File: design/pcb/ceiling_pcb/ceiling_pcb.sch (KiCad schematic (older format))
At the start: 10 parts, among them J1 Conn_01x09, J10 shock_grid, J2 Conn_01x09, J3 shock_grid, J4 shock_grid, J5 shock_grid, J6 shock_grid, J7 shock_grid, J8 shock_grid, J9 shock_grid

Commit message: Updated electrode_vertices.py to also generate electrodes interleaved along the long axis, for an orthogonal set of ceiling electrodes. New *_lengthwise footprint should be correct, if not a little wide.
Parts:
- J10, J3, J4, J5, J6, J7, J8, J9: footprint footprints:electrodes_clearance0.6mm -> footprints:electrodes_clearance0.6mm_W0.4mm_lengthwise
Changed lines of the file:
@@
 F 0 "J3" H 5378 1728 60  0000 L CNN
 F 1 "shock_grid" H 5378 1622 60  0000 L CNN
-F 2 "footprints:electrodes_clearance0.6mm" H 4350 1450 60  0001 C CNN
+F 2 "footprints:electrodes_clearance0.6mm_W0.4mm_lengthwise" H 4350 1450 60  0001 C CNN
 F 3 "" H 4350 1450 60  0001 C CNN
 	1    4350 1450
@@
 F 0 "J5" H 5378 3178 60  0000 L CNN
 F 1 "shock_grid" H 5378 3072 60  0000 L CNN
-F 2 "footprints:electrodes_clearance0.6mm" H 4350 2900 60  0001 C CNN
+F 2 "footprints:electrodes_clearance0.6mm_W0.4mm_lengthwise" H 4350 2900 60  0001 C CNN
 F 3 "" H 4350 2900 60  0001 C CNN
 	1    4350 2900
@@
 F 0 "J4" H 8478 1728 60  0000 L CNN
 F 1 "shock_grid" H 8478 1622 60  0000 L CNN
-F 2 "footprints:electrodes_clearance0.6mm" H 7450 1450 60  0001 C CNN
+F 2 "footprints:electrodes_clearance0.6mm_W0.4mm_lengthwise" H 7450 1450 60  0001 C CNN
 F 3 "" H 7450 1450 60  0001 C CNN
 	1    7450 1450
@@
 F 0 "J6" H 8478 3178 60  0000 L CNN
 F 1 "shock_grid" H 8478 3072 60  0000 L CNN
-F 2 "footprints:electrodes_clearance0.6mm" H 7450 2900 60  0001 C CNN
+F 2 "footprints:electrodes_clearance0.6mm_W0.4mm_lengthwise" H 7450 2900 60  0001 C CNN
 F 3 "" H 7450 2900 60  0001 C CNN
 	1    7450 2900
@@
 F 0 "J7" H 5378 4578 60  0000 L CNN
 F 1 "shock_grid" H 5378 4472 60  0000 L CNN
-F 2 "footprints:electrodes_clearance0.6mm" H 4350 4300 60  0001 C CNN
+F 2 "footprints:electrodes_clearance0.6mm_W0.4mm_lengthwise" H 4350 4300 60  0001 C CNN
 F 3 "" H 4350 4300 60  0001 C CNN
 	1    4350 4300
@@
 F 0 "J8" H 8478 4578 60  0000 L CNN
 F 1 "shock_grid" H 8478 4472 60  0000 L CNN
-F 2 "footprints:electrodes_clearance0.6mm" H 7450 4300 60  0001 C CNN
+F 2 "footprints:electrodes_clearance0.6mm_W0.4mm_lengthwise" H 7450 4300 60  0001 C CNN
 F 3 "" H 7450 4300 60  0001 C CNN
 	1    7450 4300
@@
 F 0 "J9" H 5378 5728 60  0000 L CNN
 F 1 "shock_grid" H 5378 5622 60  0000 L CNN
-F 2 "footprints:electrodes_clearance0.6mm" H 4350 5450 60  0001 C CNN
+F 2 "footprints:electrodes_clearance0.6mm_W0.4mm_lengthwise" H 4350 5450 60  0001 C CNN
 F 3 "" H 4350 5450 60  0001 C CNN
 	1    4350 5450
@@
 F 0 "J10" H 8478 5728 60  0000 L CNN
 F 1 "shock_grid" H 8478 5622 60  0000 L CNN
-F 2 "footprints:electrodes_clearance0.6mm" H 7450 5450 60  0001 C CNN
+F 2 "footprints:electrodes_clearance0.6mm_W0.4mm_lengthwise" H 7450 5450 60  0001 C CNN
 F 3 "" H 7450 5450 60  0001 C CNN
 	1    7450 5450

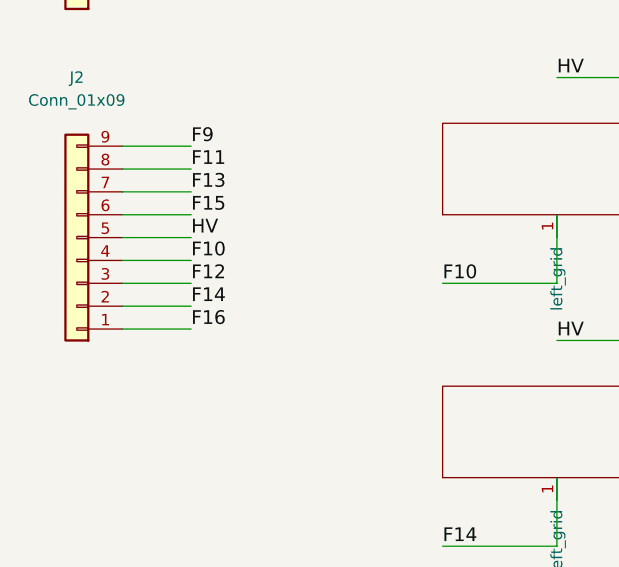
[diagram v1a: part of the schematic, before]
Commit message: Fixed bug I made in electrode vertices. Ceiling pcb pretty much done. Need to name F<N> nets consistently across Kicad projects.
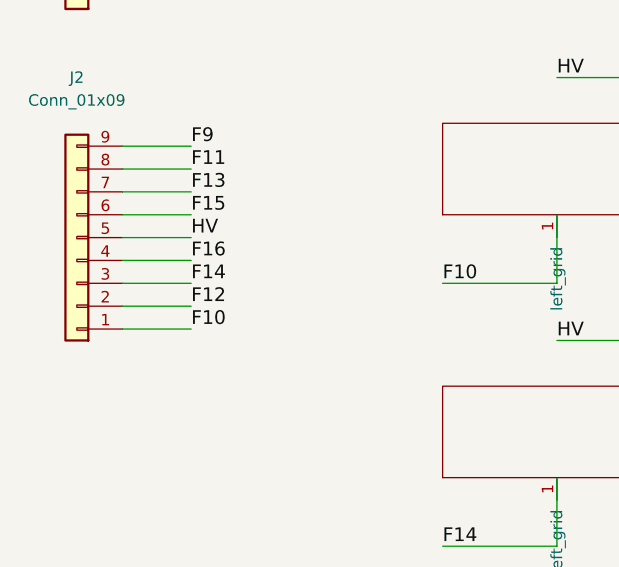
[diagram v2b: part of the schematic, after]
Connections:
- net F10: now also J2.1 (Pin_1); no longer J2.4 (Pin_4)
- net F12: now also J2.2 (Pin_2); no longer J2.3 (Pin_3)
- net F14: now also J2.3 (Pin_3); no longer J2.2 (Pin_2)
- net F16: now also J2.4 (Pin_4); no longer J2.1 (Pin_1)
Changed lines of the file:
@@
 F15
 Text Label 2250 4700 0    60   ~ 0
+F16
+Text Label 2250 4800 0    60   ~ 0
+F14
+Text Label 2250 4900 0    60   ~ 0
+F12
+Text Label 2250 5000 0    60   ~ 0
 F10
-Text Label 2250 4800 0    60   ~ 0
-F12
-Text Label 2250 4900 0    60   ~ 0
-F14
-Text Label 2250 5000 0    60   ~ 0
-F16
 Text Label 3850 5050 0    60   ~ 0
 HV

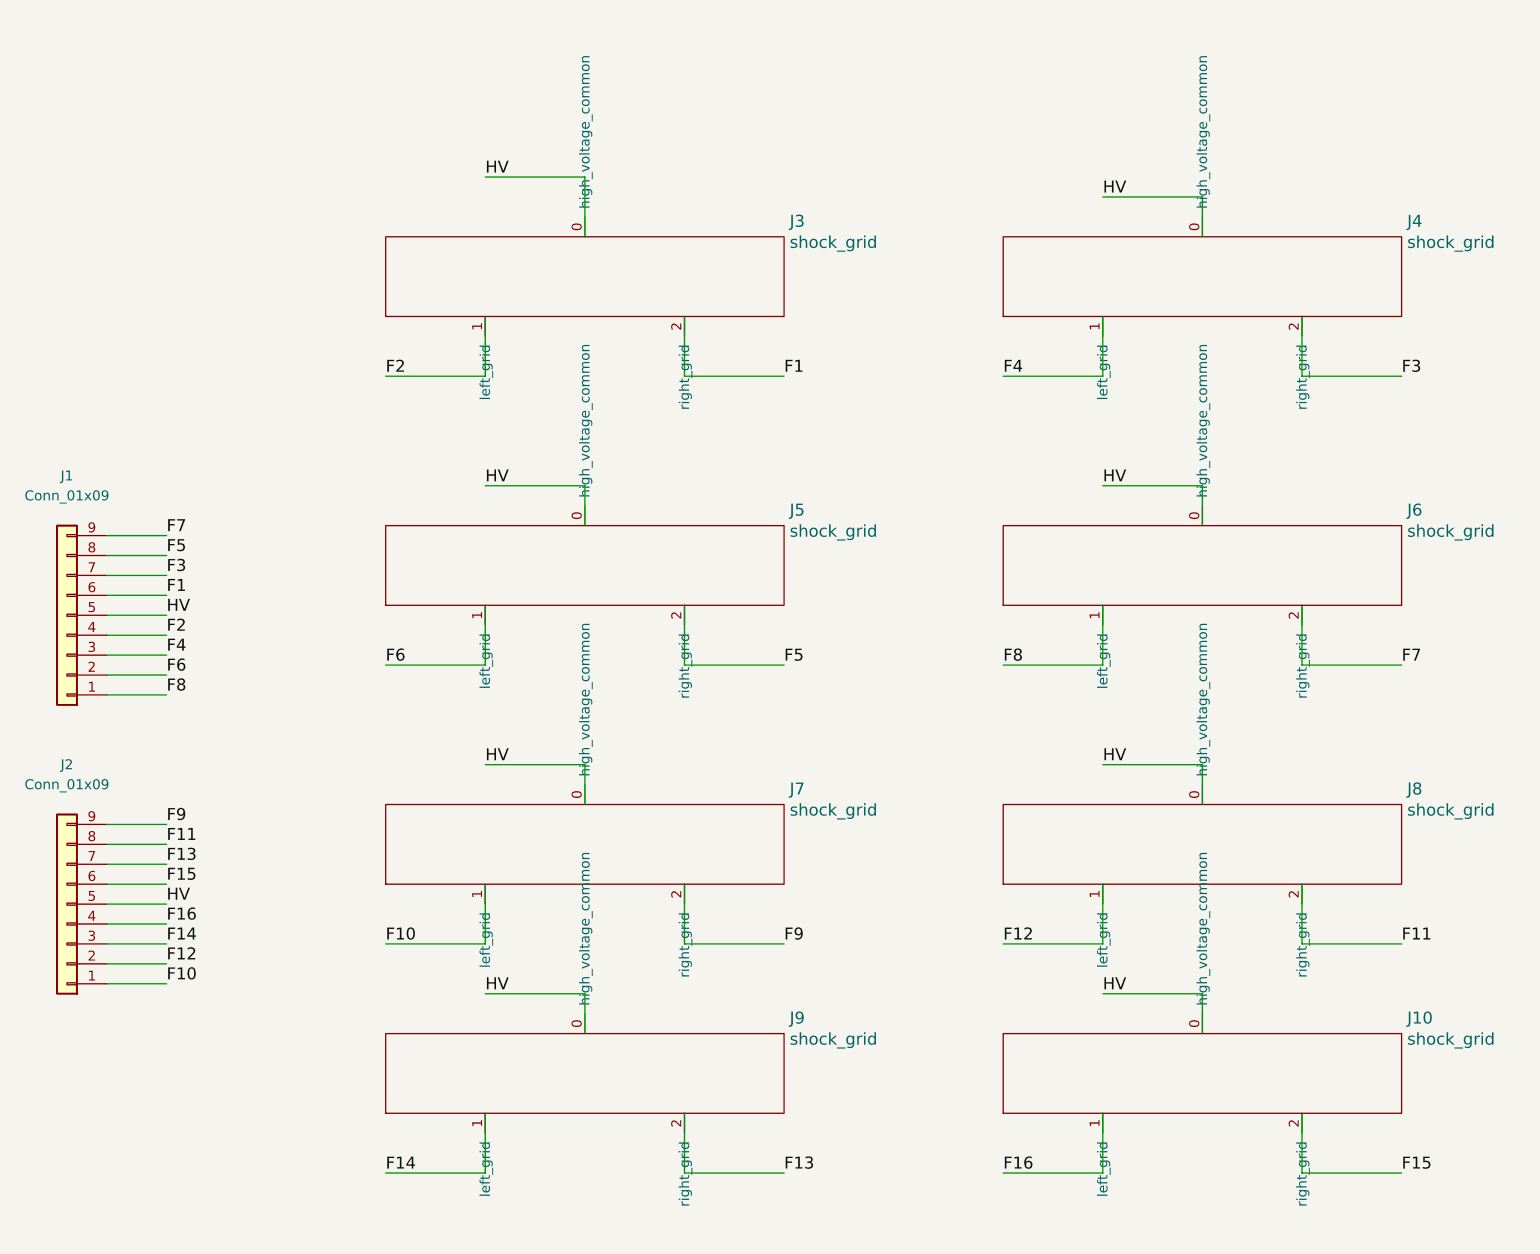
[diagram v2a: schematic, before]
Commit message: Seem to have make_board working to align top and bottom connectors, and J3 on the bottom, but I need to pick different offsets from nearest grid for top and bottom. May need to make ceiling board a little longer on the top. ADD EXTRA MOUNTING HOLES IN BOTTOM.
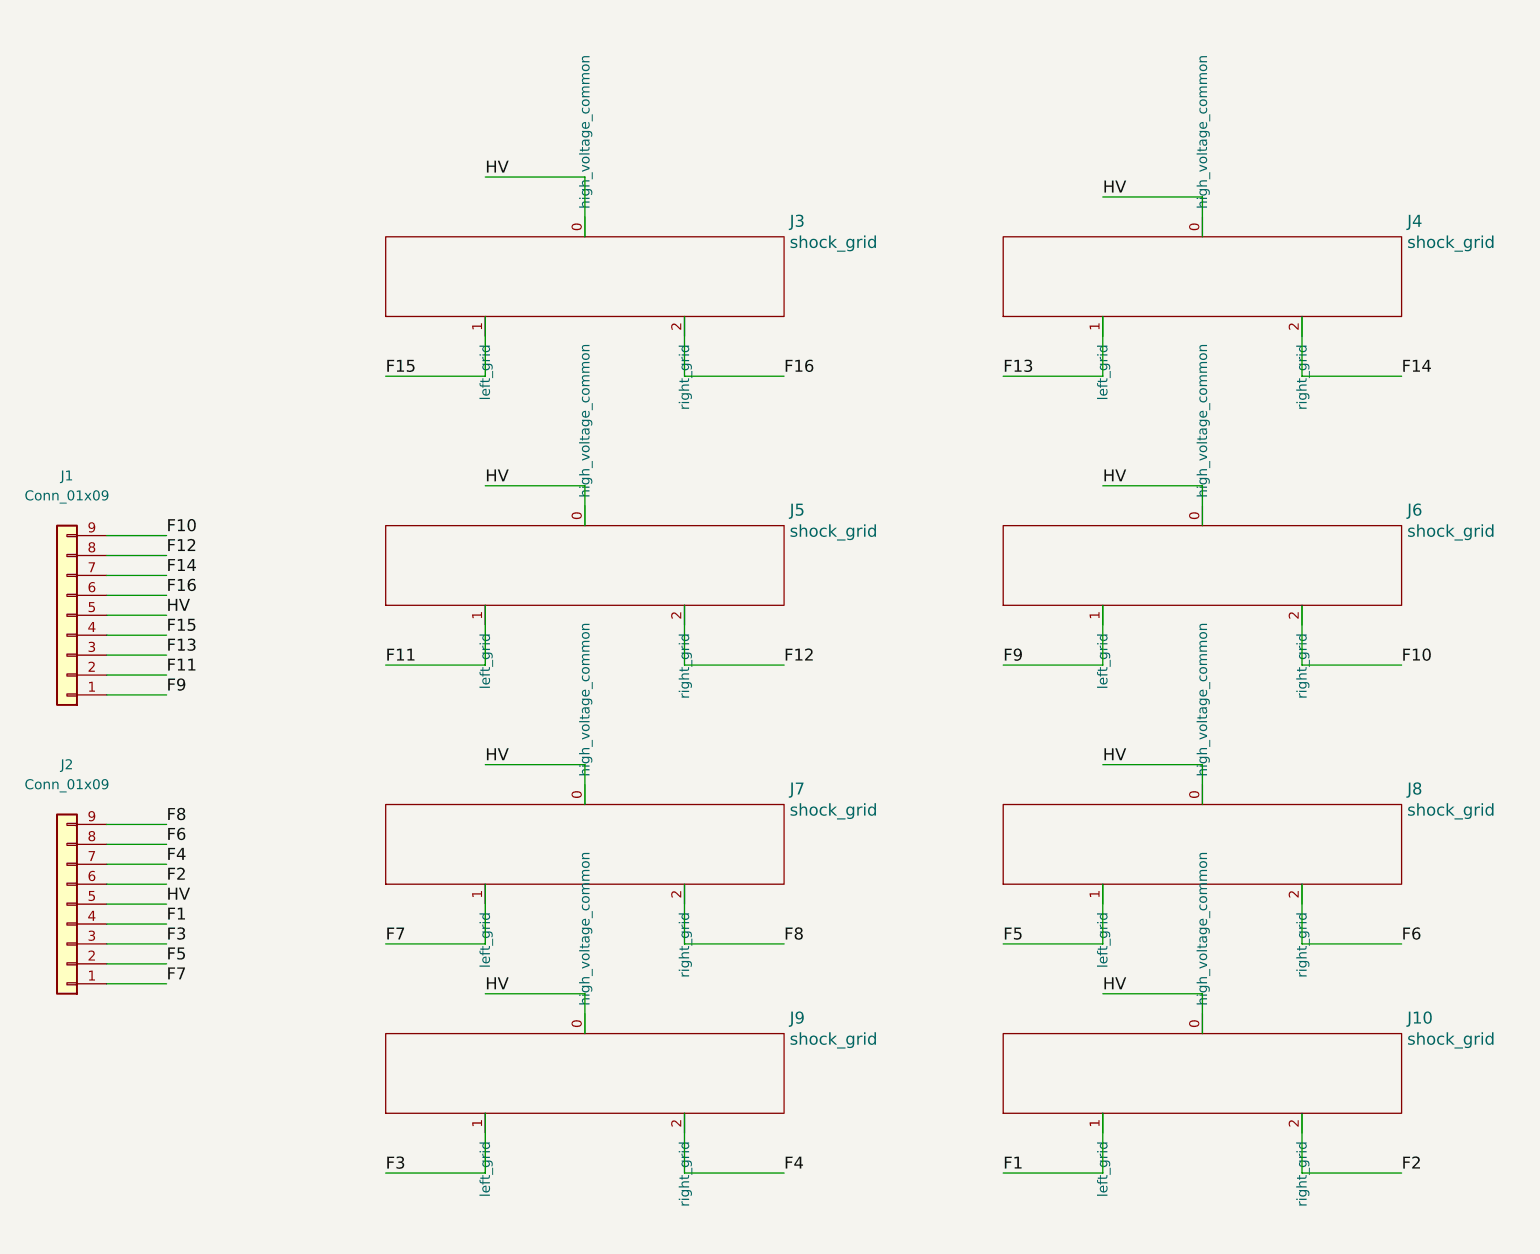
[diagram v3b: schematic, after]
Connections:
- net F1: now also J10.1 (left_grid), J2.4 (Pin_4); no longer J1.6 (Pin_6), J3.2 (right_grid)
- net F10: now also J1.9 (Pin_9), J6.2 (right_grid); no longer J2.1 (Pin_1), J7.1 (left_grid)
- net F11: now also J1.2 (Pin_2), J5.1 (left_grid); no longer J2.8 (Pin_8), J8.2 (right_grid)
- net F12: now also J1.8 (Pin_8), J5.2 (right_grid); no longer J2.2 (Pin_2), J8.1 (left_grid)
- net F13: now also J1.3 (Pin_3), J4.1 (left_grid); no longer J2.7 (Pin_7), J9.2 (right_grid)
- net F14: now also J1.7 (Pin_7), J4.2 (right_grid); no longer J2.3 (Pin_3), J9.1 (left_grid)
- net F15: now also J1.4 (Pin_4), J3.1 (left_grid); no longer J10.2 (right_grid), J2.6 (Pin_6)
- net F16: now also J1.6 (Pin_6), J3.2 (right_grid); no longer J10.1 (left_grid), J2.4 (Pin_4)
- net F2: now also J10.2 (right_grid), J2.6 (Pin_6); no longer J1.4 (Pin_4), J3.1 (left_grid)
- net F3: now also J2.3 (Pin_3), J9.1 (left_grid); no longer J1.7 (Pin_7), J4.2 (right_grid)
- net F4: now also J2.7 (Pin_7), J9.2 (right_grid); no longer J1.3 (Pin_3), J4.1 (left_grid)
- net F5: now also J2.2 (Pin_2), J8.1 (left_grid); no longer J1.8 (Pin_8), J5.2 (right_grid)
- net F6: now also J2.8 (Pin_8), J8.2 (right_grid); no longer J1.2 (Pin_2), J5.1 (left_grid)
- net F7: now also J2.1 (Pin_1), J7.1 (left_grid); no longer J1.9 (Pin_9), J6.2 (right_grid)
- net F8: now also J2.9 (Pin_9), J7.2 (right_grid); no longer J1.1 (Pin_1), J6.1 (left_grid)
- net F9: now also J1.1 (Pin_1), J6.1 (left_grid); no longer J2.9 (Pin_9), J7.2 (right_grid)
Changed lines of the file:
@@
 HV
 Text Label 2250 2750 0    60   ~ 0
+F10
+Text Label 2250 2850 0    60   ~ 0
+F12
+Text Label 2250 2950 0    60   ~ 0
+F14
+Text Label 2250 3050 0    60   ~ 0
+F16
+Text Label 2250 3250 0    60   ~ 0
+F15
+Text Label 2250 3350 0    60   ~ 0
+F13
+Text Label 2250 3450 0    60   ~ 0
+F11
+Text Label 2250 3550 0    60   ~ 0
+F9
+Text Label 2250 4200 0    60   ~ 0
+F8
+Text Label 2250 4300 0    60   ~ 0
+F6
+Text Label 2250 4400 0    60   ~ 0
+F4
+Text Label 2250 4500 0    60   ~ 0
+F2
+Text Label 2250 4700 0    60   ~ 0
+F1
+Text Label 2250 4800 0    60   ~ 0
+F3
+Text Label 2250 4900 0    60   ~ 0
+F5
+Text Label 2250 5000 0    60   ~ 0
 F7
-Text Label 2250 2850 0    60   ~ 0
-F5
-Text Label 2250 2950 0    60   ~ 0
-F3
-Text Label 2250 3050 0    60   ~ 0
-F1
-Text Label 2250 3250 0    60   ~ 0
-F2
-Text Label 2250 3350 0    60   ~ 0
-F4
-Text Label 2250 3450 0    60   ~ 0
-F6
-Text Label 2250 3550 0    60   ~ 0
-F8
-Text Label 2250 4200 0    60   ~ 0
-F9
-Text Label 2250 4300 0    60   ~ 0
-F11
-Text Label 2250 4400 0    60   ~ 0
-F13
-Text Label 2250 4500 0    60   ~ 0
-F15
-Text Label 2250 4700 0    60   ~ 0
-F16
-Text Label 2250 4800 0    60   ~ 0
-F14
-Text Label 2250 4900 0    60   ~ 0
-F12
-Text Label 2250 5000 0    60   ~ 0
-F10
 Text Label 3850 5050 0    60   ~ 0
 HV
@@
 HV
 Text Label 3350 1950 0    60   ~ 0
+F15
+Text Label 5350 1950 0    60   ~ 0
+F16
+Text Label 6450 1950 0    60   ~ 0
+F13
+Text Label 8450 1950 0    60   ~ 0
+F14
+Text Label 3350 3400 0    60   ~ 0
+F11
+Text Label 5350 3400 0    60   ~ 0
+F12
+Text Label 6450 3400 0    60   ~ 0
+F9
+Text Label 8450 3400 0    60   ~ 0
+F10
+Text Label 3350 4800 0    60   ~ 0
+F7
+Text Label 5350 4800 0    60   ~ 0
+F8
+Text Label 6450 4800 0    60   ~ 0
+F5
+Text Label 8450 4800 0    60   ~ 0
+F6
+Text Label 8450 5950 0    60   ~ 0
 F2
-Text Label 5350 1950 0    60   ~ 0
+Text Label 6450 5950 0    60   ~ 0
 F1
-Text Label 6450 1950 0    60   ~ 0
+Text Label 3350 5950 0    60   ~ 0
+F3
+Text Label 5350 5950 0    60   ~ 0
 F4
-Text Label 8450 1950 0    60   ~ 0
-F3
-Text Label 3350 3400 0    60   ~ 0
-F6
-Text Label 5350 3400 0    60   ~ 0
-F5
-Text Label 6450 3400 0    60   ~ 0
-F8
-Text Label 8450 3400 0    60   ~ 0
-F7
-Text Label 3350 4800 0    60   ~ 0
-F10
-Text Label 5350 4800 0    60   ~ 0
-F9
-Text Label 6450 4800 0    60   ~ 0
-F12
-Text Label 8450 4800 0    60   ~ 0
-F11
-Text Label 8450 5950 0    60   ~ 0
-F15
-Text Label 6450 5950 0    60   ~ 0
-F16
-Text Label 3350 5950 0    60   ~ 0
-F14
-Text Label 5350 5950 0    60   ~ 0
-F13
 Wire Wire Line
 	4350 950  4350 1250

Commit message: Before pushing attempt at fixing ceiling through EEschema load / save.
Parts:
- J1, J2: symbol Conn_01x09 -> ceiling_pcb:Conn_01x09
- J10, J3, J4, J5, J6, J7, J8, J9: symbol shock_grid -> shock_electrodes:shock_grid
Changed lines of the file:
@@
-EESchema Schematic File Version 3
-LIBS:Connector
-LIBS:shock_grid
+EESchema Schematic File Version 4
 LIBS:ceiling_pcb-cache
 EELAYER 26 0
@@
 $EndDescr
 $Comp
-L shock_grid J3
+L shock_electrodes:shock_grid J3
 U 1 1 59F778B5
 P 4350 1450
@@
 $EndComp
 $Comp
-L shock_grid J5
+L shock_electrodes:shock_grid J5
 U 1 1 59F779C5
 P 4350 2900
@@
 $EndComp
 $Comp
-L shock_grid J4
+L shock_electrodes:shock_grid J4
 U 1 1 59F77CE3
 P 7450 1450
@@
 $EndComp
 $Comp
-L shock_grid J6
+L shock_electrodes:shock_grid J6
 U 1 1 59F77DC7
 P 7450 2900
@@
 $EndComp
 $Comp
-L shock_grid J7
+L shock_electrodes:shock_grid J7
 U 1 1 59F77FF1
 P 4350 4300
@@
 $EndComp
 $Comp
-L shock_grid J8
+L shock_electrodes:shock_grid J8
 U 1 1 59F780F5
 P 7450 4300
@@
 $EndComp
 $Comp
-L shock_grid J9
+L shock_electrodes:shock_grid J9
 U 1 1 59F78242
 P 4350 5450
@@
 $EndComp
 $Comp
-L shock_grid J10
+L shock_electrodes:shock_grid J10
 U 1 1 59F7866D
 P 7450 5450
@@
 $EndComp
 $Comp
-L Conn_01x09 J1
+L ceiling_pcb:Conn_01x09 J1
 U 1 1 59F76D5B
 P 1750 3150
@@
 	4850 1950 5350 1950
 $Comp
-L Conn_01x09 J2
+L ceiling_pcb:Conn_01x09 J2
 U 1 1 5A268DBE
 P 1750 4600
